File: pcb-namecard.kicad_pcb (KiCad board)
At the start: 2 copper layers, 98.9 x 55 mm, 16 parts, among them J1 USB_IN, J2 OUT, J3 USB_AUX, SW1 DOWN, SW2 UP, U1 LM317L

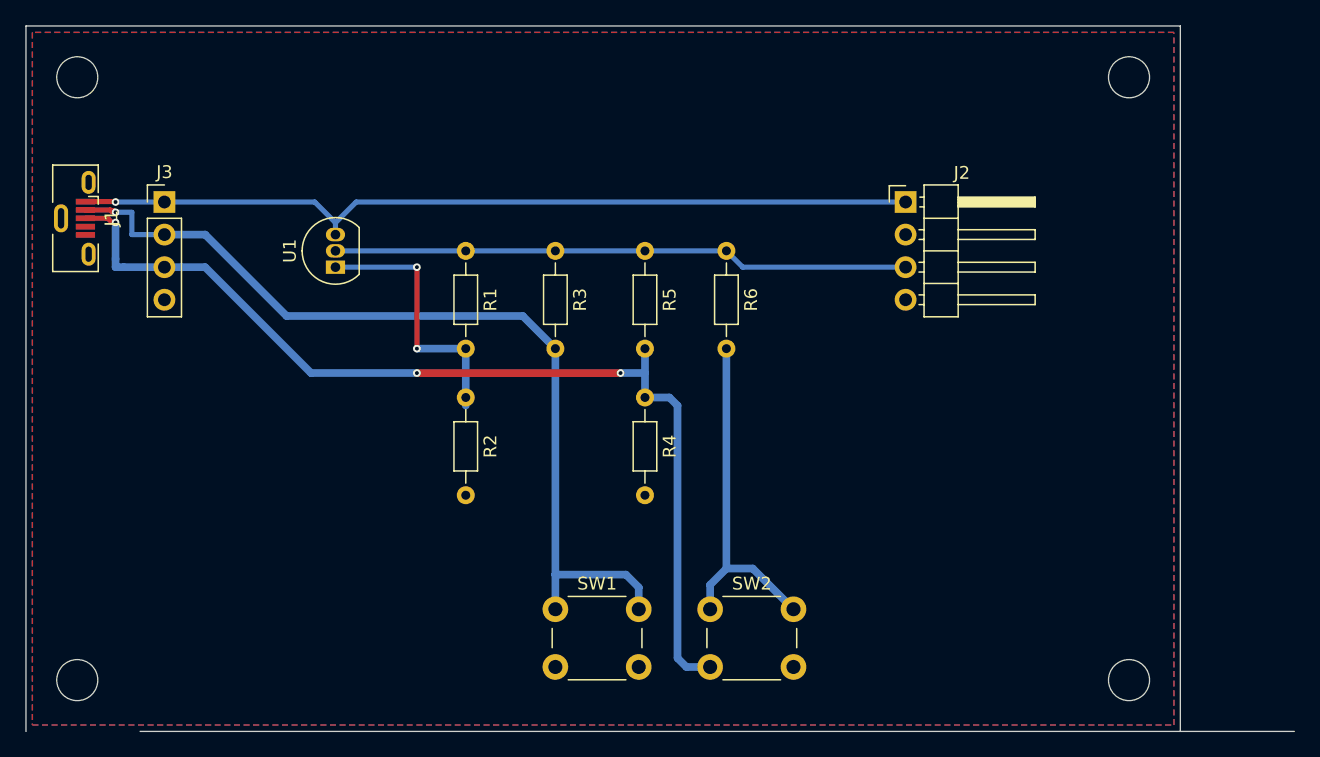
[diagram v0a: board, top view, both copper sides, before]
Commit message: - Backported to KiCad v4 - Added INIT button to enter QC3.0 mode - Revised register values
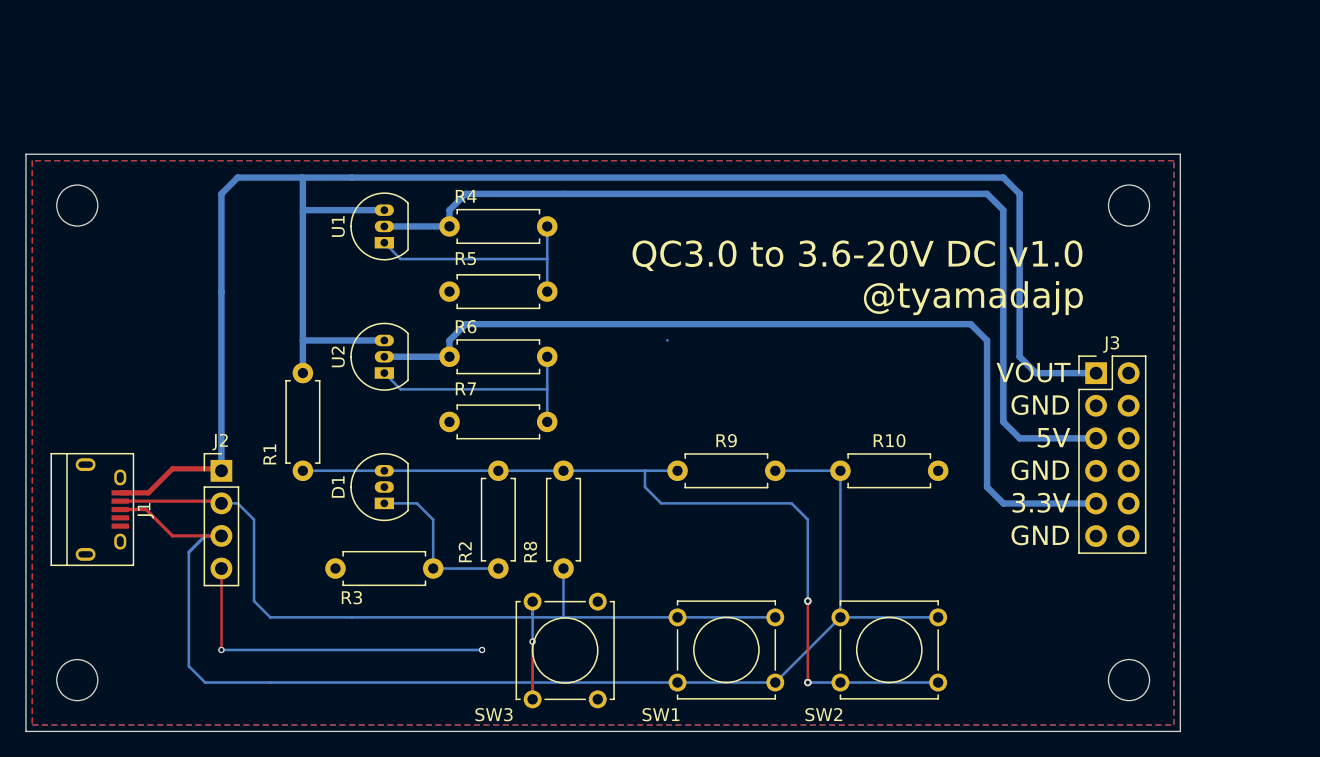
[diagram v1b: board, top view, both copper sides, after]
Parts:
- added D1: TL431, TO_SOT_Packages_THT:TO-92_Inline_Narrow_Oval, F.Cu at (118.1, 108.0)
- added R10: 3.3K, Resistors_THT:R_Axial_DIN0207_L6.3mm_D2.5mm_P7.62mm_Horizontal, F.Cu at (153.7, 105.4)
- added R7: 330, Resistors_THT:R_Axial_DIN0207_L6.3mm_D2.5mm_P7.62mm_Horizontal, F.Cu at (130.8, 101.6)
- added R8: 10K, Resistors_THT:R_Axial_DIN0207_L6.3mm_D2.5mm_P7.62mm_Horizontal, F.Cu at (132.1, 105.4)
- added R9: 10K, Resistors_THT:R_Axial_DIN0207_L6.3mm_D2.5mm_P7.62mm_Horizontal, F.Cu at (141.0, 105.4)
- added SW3: INIT, Buttons_Switches_THT:SW_Tactile_Straight_KSA0Axx1LFTR, F.Cu at (129.7, 123.2)
- added U2: LM317, TO_SOT_Packages_THT:TO-92_Inline_Narrow_Oval, F.Cu at (118.1, 97.8)
- J1: value USB_IN -> USB_OTG; footprint Connector_USB:USB_Micro-B_Molex-105133-0001 -> Connectors:USB_Micro-B
- J2: value OUT -> USB_ALT; footprint Connector_PinHeader_2.54mm:PinHeader_1x04_P2.54mm_Horizontal -> Pin_Headers:Pin_Header_Straight_1x04_Pitch2.54mm
- J3: value USB_AUX -> POWER_OUT; footprint Connector_PinHeader_2.54mm:PinHeader_1x04_P2.54mm_Vertical -> Pin_Headers:Pin_Header_Straight_2x06_Pitch2.54mm
- MH1, MH2, MH3, MH4: value MountingHole_3.2mm_M3 -> M3
- R1: value 47K -> 100; footprint Resistor_THT:R_Axial_DIN0204_L3.6mm_D1.6mm_P7.62mm_Horizontal -> Resistors_THT:R_Axial_DIN0207_L6.3mm_D2.5mm_P7.62mm_Horizontal
- R2: value 47K -> 3.3K; footprint Resistor_THT:R_Axial_DIN0204_L3.6mm_D1.6mm_P7.62mm_Horizontal -> Resistors_THT:R_Axial_DIN0207_L6.3mm_D2.5mm_P7.62mm_Horizontal
- R3: value 47K -> 10K; footprint Resistor_THT:R_Axial_DIN0204_L3.6mm_D1.6mm_P7.62mm_Horizontal -> Resistors_THT:R_Axial_DIN0207_L6.3mm_D2.5mm_P7.62mm_Horizontal
- R4: value 10K -> 330; footprint Resistor_THT:R_Axial_DIN0204_L3.6mm_D1.6mm_P7.62mm_Horizontal -> Resistors_THT:R_Axial_DIN0207_L6.3mm_D2.5mm_P7.62mm_Horizontal
- R5: value 47K -> 1K; footprint Resistor_THT:R_Axial_DIN0204_L3.6mm_D1.6mm_P7.62mm_Horizontal -> Resistors_THT:R_Axial_DIN0207_L6.3mm_D2.5mm_P7.62mm_Horizontal
- R6: value 1K -> 220; footprint Resistor_THT:R_Axial_DIN0204_L3.6mm_D1.6mm_P7.62mm_Horizontal -> Resistors_THT:R_Axial_DIN0207_L6.3mm_D2.5mm_P7.62mm_Horizontal
- SW1, SW2: footprint Button_Switch_THT:SW_PUSH_6mm -> Buttons_Switches_THT:SW_Tactile_Straight_KSA0Axx1LFTR
- U1: value LM317L -> LM317; footprint Package_TO_SOT_THT:TO-92_Inline -> TO_SOT_Packages_THT:TO-92_Inline_Narrow_Oval
- moved J3 73.9 mm to (173.6, 97.8)
- moved J2 57.3 mm to (105.4, 105.4)
- moved R3 26.5 mm to (121.9, 113.0), turned to 180 degrees
- moved R6 23.1 mm to (123.2, 96.5), turned to 0 degrees
- moved J1 22.8 mm to (96.2, 108.4)
- moved R4 20.3 mm to (123.2, 86.4), turned to 0 degrees
- moved R1 15.9 mm to (111.8, 97.8)
- moved SW2 10.2 mm to (153.7, 116.8)
- moved MH1 10.0 mm to (94.2, 84.7)
- moved MH2 10.0 mm to (176.2, 84.7)
- moved SW1 9.55 mm to (141.0, 116.8)
- moved R5 8.26 mm to (130.8, 91.4), turned to 180 degrees
- moved R2 6.25 mm to (127.0, 105.4)
- moved U1 4.26 mm to (118.1, 87.6)
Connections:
- J2 pad 2: GND -> Net-(J1-Pad2)
- J2 pad 3: Net-(J2-Pad3) -> Net-(J1-Pad3)
- J3 pad 2: Net-(J1-Pad2) -> Net-(J1-Pad1)
- J3 pad 3: Net-(J1-Pad3) -> GND
- R1 pad 1: Net-(J2-Pad3) -> Net-(J1-Pad1)
- R1 pad 2: Net-(R1-Pad2) -> Net-(D1-Pad3)
- R2 pad 1: Net-(R1-Pad2) -> Net-(D1-Pad3)
- R2 pad 2: GND -> Net-(D1-Pad1)
- R3 pad 1: Net-(J2-Pad3) -> Net-(D1-Pad1)
- R3 pad 2: Net-(J1-Pad2) -> GND
- R4 pad 1: Net-(J1-Pad3) -> Net-(J3-Pad5)
- R4 pad 2: GND -> Net-(R4-Pad2)
- R5 pad 1: Net-(J2-Pad3) -> Net-(R4-Pad2)
- R5 pad 2: Net-(J1-Pad3) -> GND
- R6 pad 1: Net-(J2-Pad3) -> Net-(J3-Pad10)
- SW1 pad 2: GND -> Net-(J1-Pad3)
- SW2 pad 1: Net-(R6-Pad2) -> Net-(J1-Pad3)
- SW2 pad 2: Net-(J1-Pad3) -> Net-(D1-Pad3)
- U1 pad 1: Net-(R1-Pad2) -> Net-(R4-Pad2)
- U1 pad 2: Net-(J2-Pad3) -> Net-(J3-Pad5)
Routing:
- net Net-(J3-Pad5): track 0.00 -> 74.9 mm
- net Net-(J1-Pad1): track 66.3 -> 141.0 mm, vias 1 -> 0
- net Net-(J3-Pad10): track 0.00 -> 69.8 mm
- net Net-(D1-Pad3): track 0.00 -> 67.1 mm, vias 0 -> 2
- net Net-(J2-Pad3): track 45.0 -> 0.00 mm
- net GND: track 0.00 -> 26.7 mm, vias 0 -> 2
- net Net-(R1-Pad2): track 21.0 -> 0.00 mm, vias 2 -> 0
- net Net-(J1-Pad3): track 79.5 -> 98.3 mm, vias 3 -> 0
- net Net-(R4-Pad2): track 0.00 -> 18.3 mm
- net Net-(D1-Pad1): track 0.00 -> 13.2 mm
- net Net-(R6-Pad2): track 27.4 -> 18.3 mm
- net Net-(J1-Pad2): track 71.1 -> 70.0 mm
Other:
- board size 98.9 x 55 mm -> 90 x 45 mm
- net class Default: via_drill 0.3 -> 0.4
- net class Power added: clearance 0.2, trace_width 0.4, via_dia 0.6, via_drill 0.4
- rule trace_min: 0.1524 -> 0.2
- rule via_min_drill: 0.2 -> 0.3
- board text added: "3.3V"
- board text added: "5V"
- board text added: "GND"
- board text added: "QC3.0 to 3.6-20V DC v1.0 @tyamadajp"
- board text added: "VOUT"

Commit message: - Changed USB_ALT to 01x05 connector. - Added more text to F.Silk
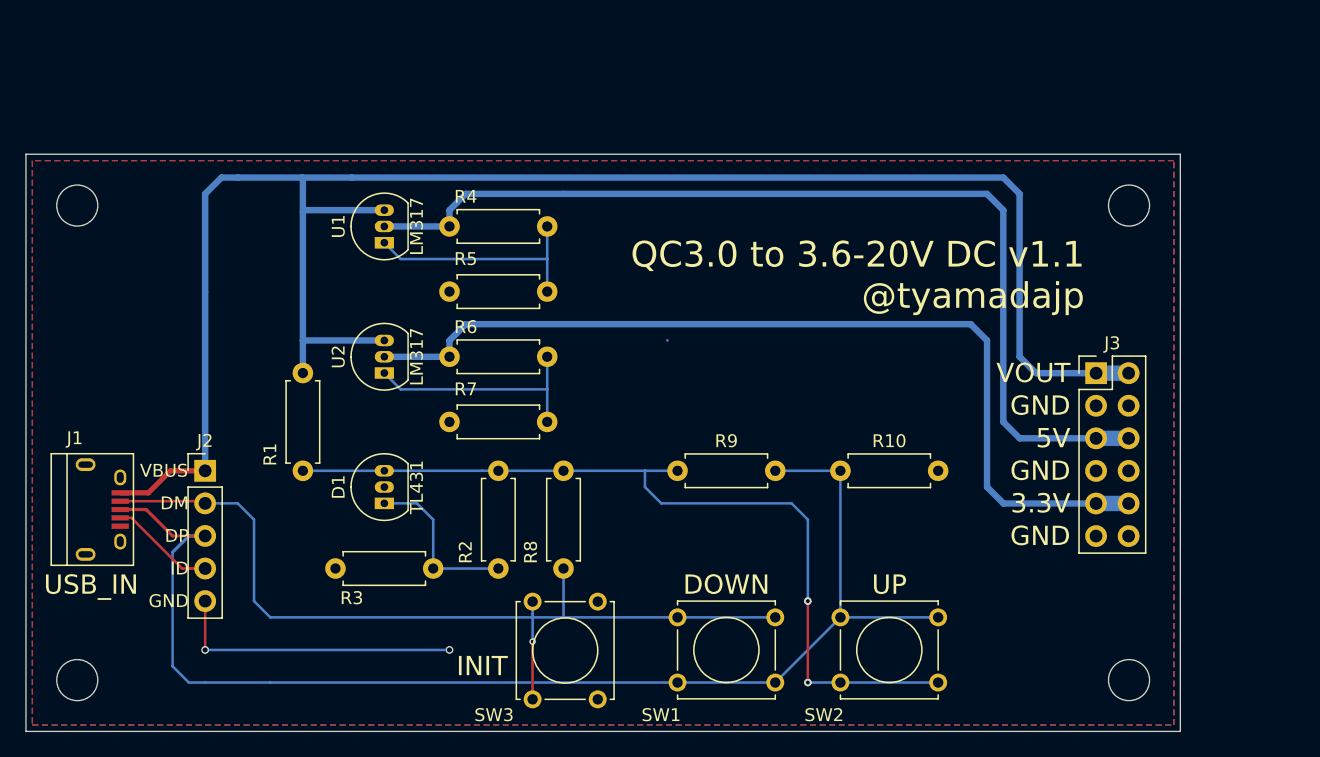
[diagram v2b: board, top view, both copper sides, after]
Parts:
- J2: footprint Pin_Headers:Pin_Header_Straight_1x04_Pitch2.54mm -> Pin_Headers:Pin_Header_Straight_1x05_Pitch2.54mm
- moved J2 1.27 mm to (104.1, 105.4)
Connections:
- J1 pad 4: GND -> Net-(J1-Pad4)
- J2 pad 4: GND -> Net-(J1-Pad4)
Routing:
- net Net-(J1-Pad4): track 0.00 -> 8.26 mm
- net GND: track 26.7 -> 23.6 mm
- net Net-(J3-Pad5): track 74.9 -> 77.4 mm
- net Net-(J3-Pad10): track 69.8 -> 72.3 mm
- net Net-(J1-Pad1): track 141.0 -> 143.5 mm
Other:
- board text added: "DM"
- board text added: "DOWN"
- board text added: "DP"
- board text added: "ID"
- board text added: "INIT"
- board text added: "LM317"
- board text added: "QC3.0 to 3.6-20V DC v1.1 @tyamadajp"
- board text added: "TL431"
- board text added: "UP"
- board text added: "USB_IN"
- board text added: "VBUS"
- board text removed: "QC3.0 to 3.6-20V DC v1.0 @tyamadajp"
